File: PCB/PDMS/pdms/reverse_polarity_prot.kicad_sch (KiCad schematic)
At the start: 5 parts, among them IC15 LM74700QDBVRQ1, Q3 IAUA250N04S6N007AUMA1

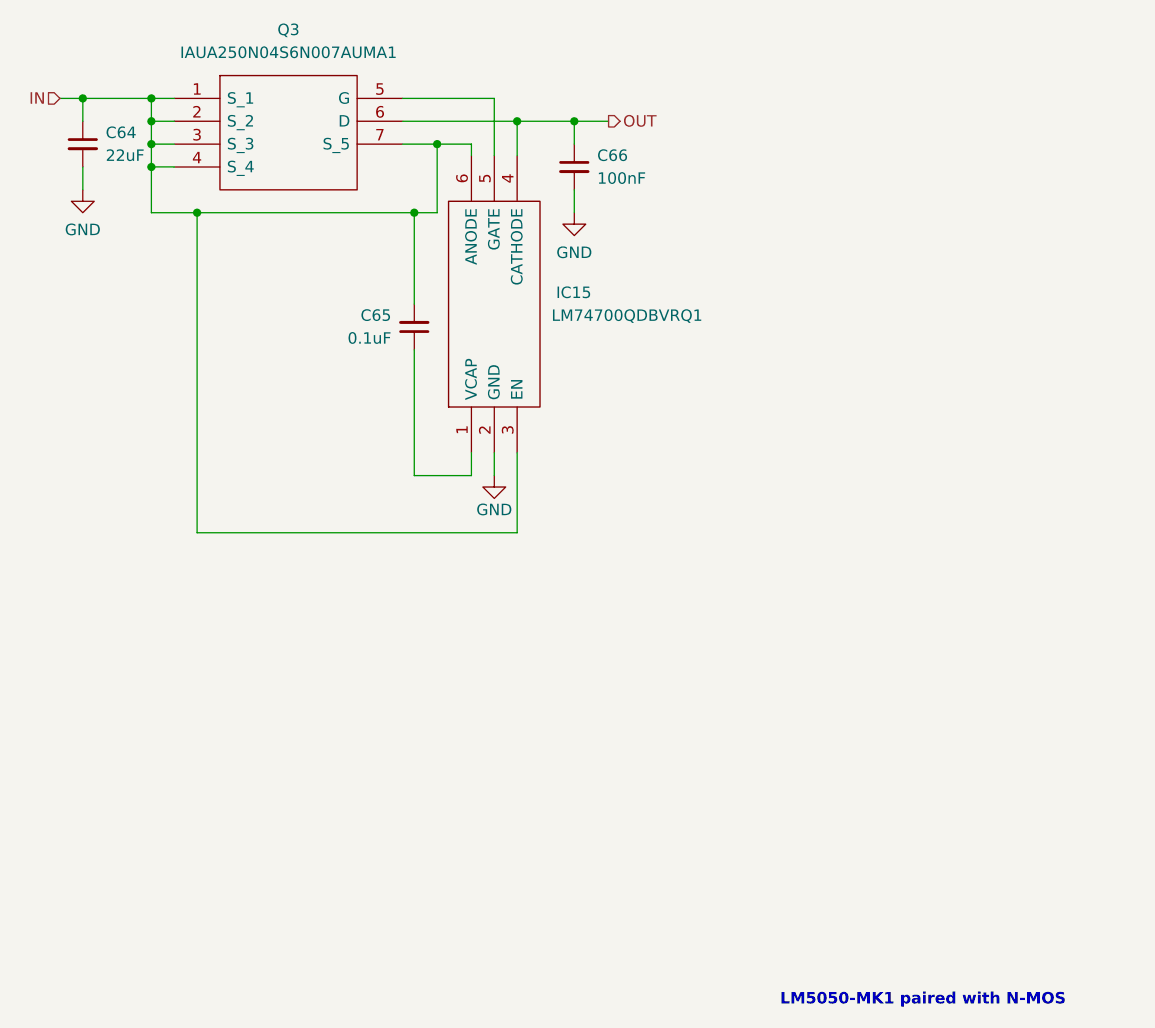
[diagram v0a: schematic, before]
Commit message: Changed symbol and footprint of LM74700
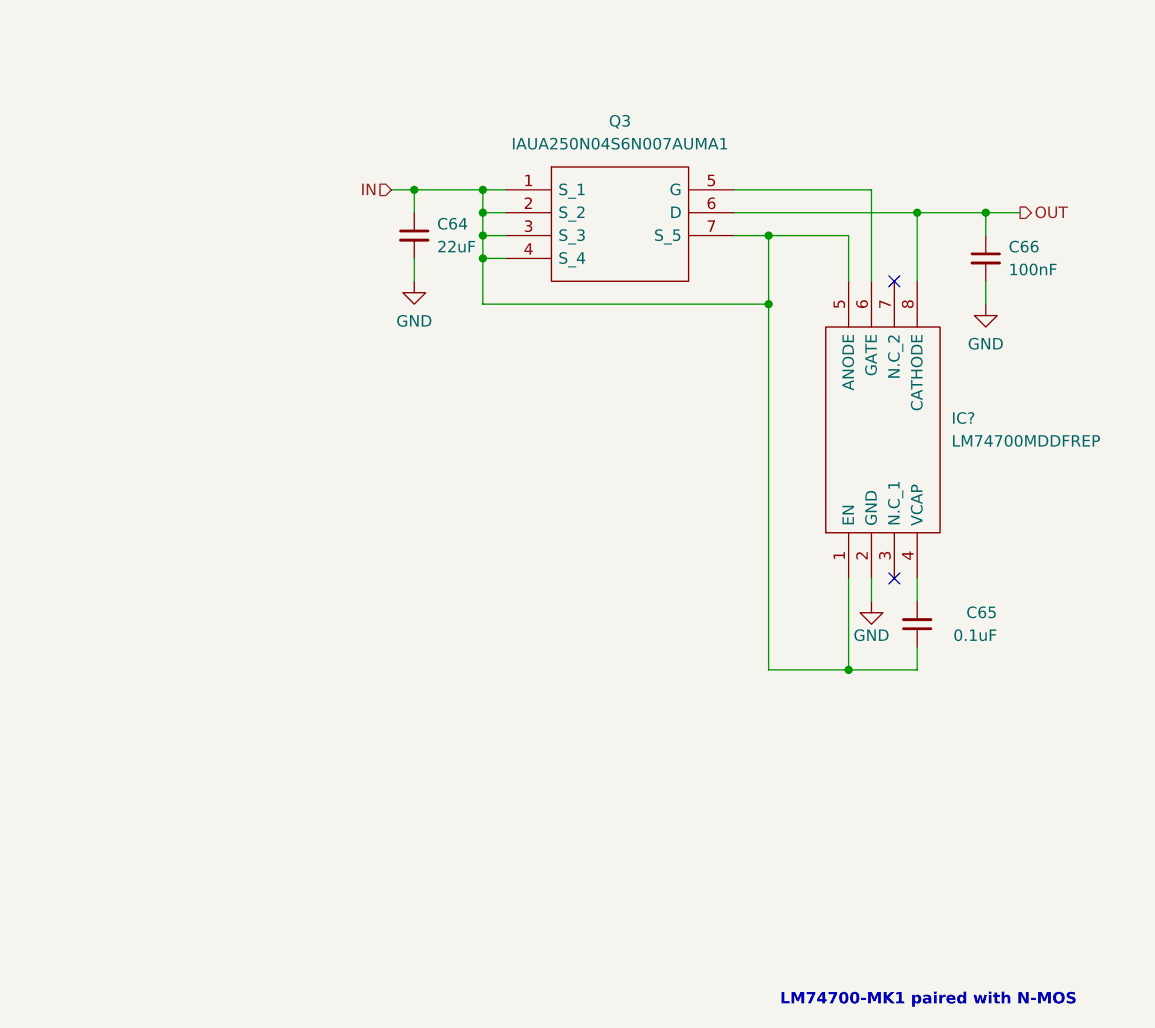
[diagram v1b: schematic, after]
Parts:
- removed IC15: LM74700QDBVRQ1, PDMS_Additional:SOT95P280X145-6N, symbol pdms_additional:LM74700QDBVRQ1
- added IC?: LM74700MDDFREP, SOT65P280X110-8N, symbol pdms_additional:LM74700MDDFREP
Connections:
- net GND: now also IC?.2 (GND)
- net IN: now also C65.1, IC?.1 (EN), IC?.5 (ANODE); no longer C65.2
- net OUT: now also IC?.8 (CATHODE)
- net at Q3.5 (G): now also IC?.6 (GATE)
- new net: C65.2, IC?.4 (VCAP)
- no-connect marks 0 -> 2
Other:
- note added: "LM74700-MK1 paired with N-MOS"
- note removed: "LM5050-MK1 paired with N-MOS"
- moved on the sheet: C64, C65, C66, Q3

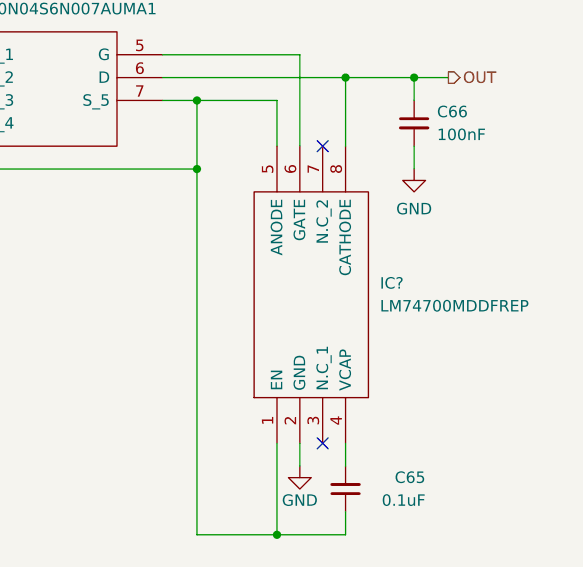
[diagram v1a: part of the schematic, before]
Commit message: Wired all peripherals
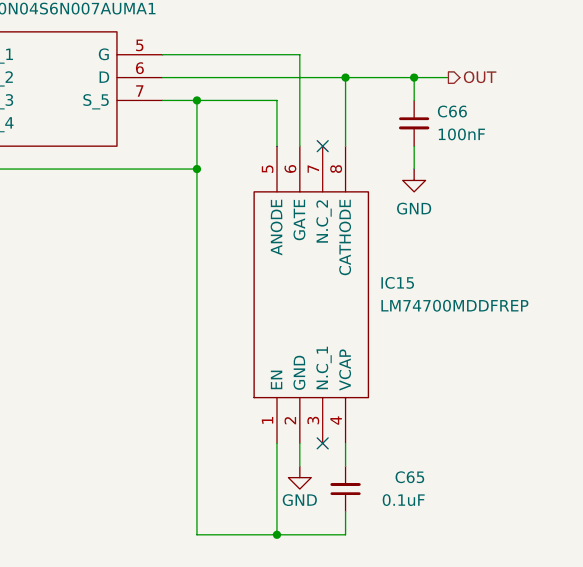
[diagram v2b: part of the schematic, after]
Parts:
- IC15: renamed from IC?; footprint SOT65P280X110-8N -> PDMS_Additional:SOT65P280X110-8N
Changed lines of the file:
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@@
   (symbol (lib_id "pdms_additional:LM74700MDDFREP") (at 107.95 81.28 90) (unit 1)
     (in_bom yes) (on_board yes) (fields_autoplaced)
-    (property "Reference" "IC?" (id 0) (at 119.38 63.4999 90)
+    (property "Reference" "IC15" (id 0) (at 119.38 63.4999 90)
       (effects (font (size 1.27 1.27)) (justify right))
     )
@@
       (effects (font (size 1.27 1.27)) (justify right))
     )
-    (property "Footprint" "SOT65P280X110-8N" (id 2) (at 105.41 52.07 0)
+    (property "Footprint" "PDMS_Additional:SOT65P280X110-8N" (id 2) (at 105.41 52.07 0)
       (effects (font (size 1.27 1.27)) (justify left) hide)
     )

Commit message: Mostly assigned footprints
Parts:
- C64, C65, C66: footprint (none) -> Capacitor_SMD:C_0402_1005Metric_Pad0.74x0.62mm_HandSolder
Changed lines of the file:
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@@
       (effects (font (size 1.27 1.27)) (justify left))
     )
-    (property "Footprint" "" (id 2) (at 59.69 43.18 0)
+    (property "Footprint" "Capacitor_SMD:C_0402_1005Metric_Pad0.74x0.62mm_HandSolder" (id 2) (at 59.69 43.18 0)
       (effects (font (size 1.27 1.27)) hide)
     )
@@
       (effects (font (size 1.27 1.27)) (justify left))
     )
-    (property "Footprint" "" (id 2) (at 123.19 45.72 0)
+    (property "Footprint" "Capacitor_SMD:C_0402_1005Metric_Pad0.74x0.62mm_HandSolder" (id 2) (at 123.19 45.72 0)
       (effects (font (size 1.27 1.27)) hide)
     )
@@
       (effects (font (size 1.27 1.27)) (justify right))
     )
-    (property "Footprint" "" (id 2) (at 115.57 86.36 0)
+    (property "Footprint" "Capacitor_SMD:C_0402_1005Metric_Pad0.74x0.62mm_HandSolder" (id 2) (at 115.57 86.36 0)
       (effects (font (size 1.27 1.27)) hide)
     )

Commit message: Added connector and more
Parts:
- C64, C66: footprint Capacitor_SMD:C_0402_1005Metric_Pad0.74x0.62mm_HandSolder -> Capacitor_SMD:C_0805_2012Metric
- C65: footprint Capacitor_SMD:C_0402_1005Metric_Pad0.74x0.62mm_HandSolder -> Resistor_SMD:R_0402_1005Metric
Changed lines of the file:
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@@
       (effects (font (size 1.27 1.27)) (justify left))
     )
-    (property "Footprint" "Capacitor_SMD:C_0402_1005Metric_Pad0.74x0.62mm_HandSolder" (id 2) (at 59.69 43.18 0)
+    (property "Footprint" "Capacitor_SMD:C_0805_2012Metric" (id 2) (at 59.69 43.18 0)
       (effects (font (size 1.27 1.27)) hide)
     )
@@
       (effects (font (size 1.27 1.27)) (justify left))
     )
-    (property "Footprint" "Capacitor_SMD:C_0402_1005Metric_Pad0.74x0.62mm_HandSolder" (id 2) (at 123.19 45.72 0)
+    (property "Footprint" "Capacitor_SMD:C_0805_2012Metric" (id 2) (at 123.19 45.72 0)
       (effects (font (size 1.27 1.27)) hide)
     )
@@
       (effects (font (size 1.27 1.27)) (justify right))
     )
-    (property "Footprint" "Capacitor_SMD:C_0402_1005Metric_Pad0.74x0.62mm_HandSolder" (id 2) (at 115.57 86.36 0)
+    (property "Footprint" "Resistor_SMD:R_0402_1005Metric" (id 2) (at 115.57 86.36 0)
       (effects (font (size 1.27 1.27)) hide)
     )
